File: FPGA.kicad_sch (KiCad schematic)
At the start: 2 parts

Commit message: added most of the sourcing info
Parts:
- D3: Source (none) -> https://onecall.farnell.com/multicomp-pro/ss13l/schottky-re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
- FPGA1: Source (none) -> completed it mate
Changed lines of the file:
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@@
+      (effects (font (size 1.27 1.27)) hide)
+    )
+    (property "Source" "https://onecall.farnell.com/multicomp-pro/ss13l/schottky-rect-single-30v-sod-123fl/dp/3883704" (id 4) (at 107.95 121.92 0)
       (effects (font (size 1.27 1.27)) hide)
     )
@@
       (effects (font (size 1.27 1.27)) hide)
     )
+    (property "Source" "completed it mate" (id 4) (at 140.97 87.63 0)
+      (effects (font (size 1.27 1.27)) hide)
+    )

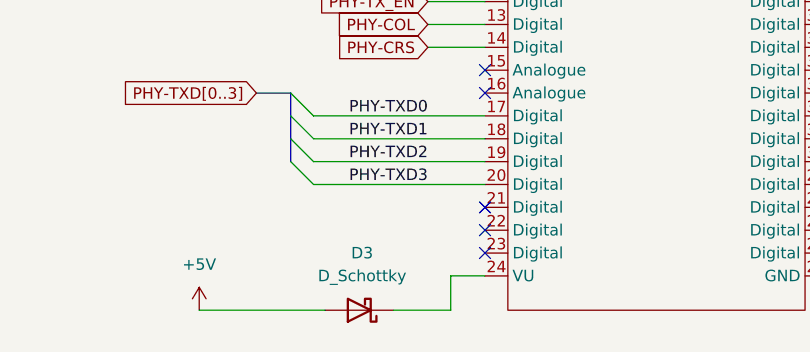
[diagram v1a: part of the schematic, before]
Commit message: solved power drc problems
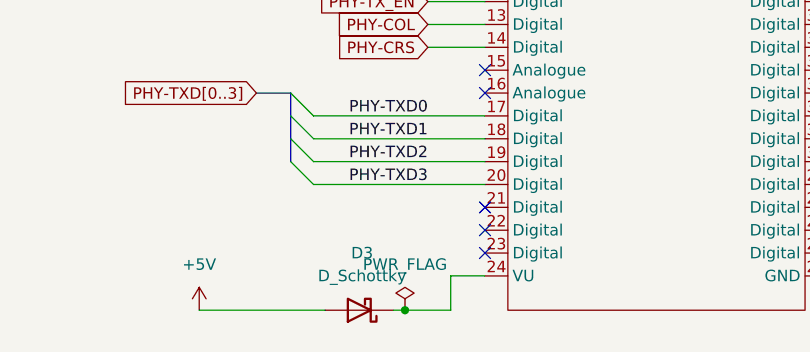
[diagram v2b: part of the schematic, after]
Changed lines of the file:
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@@
 (kicad_sch (version 20211123) (generator eeschema)
   (paper "A4")
+  (junction (at 113.03 121.92) (diameter 0) (color 0 0 0 0)
+  )
   (no_connect (at 160.02 95.25))
   (no_connect (at 121.92 97.79))
@@
     (stroke (width 0) (type default) (color 0 0 0 0))
   )
+  (wire (pts (xy 113.03 121.92) (xy 111.76 121.92))
+    (stroke (width 0) (type default) (color 0 0 0 0))
+  )
   (bus (pts (xy 91.44 64.77) (xy 91.44 67.31))
     (stroke (width 0) (type default) (color 0 0 0 0))
@@
     (stroke (width 0) (type default) (color 0 0 0 0))
   )
-  (wire (pts (xy 118.11 121.92) (xy 111.76 121.92))
+  (wire (pts (xy 118.11 121.92) (xy 113.03 121.92))
     (stroke (width 0) (type default) (color 0 0 0 0))
   )
@@
     (pin "9")
   )
+  (symbol (lib_id "power:PWR_FLAG") (at 113.03 121.92 0) (unit 1)
+    (in_bom yes) (on_board yes) (fields_autoplaced)
+    (property "Reference" "#FLG0111" (id 0) (at 113.03 120.015 0)
+      (effects (font (size 1.27 1.27)) hide)
+    )
+    (property "Value" "PWR_FLAG" (id 1) (at 113.03 116.84 0))
+    (property "Footprint" "" (id 2) (at 113.03 121.92 0)
+      (effects (font (size 1.27 1.27)) hide)
+    )
+    (property "Datasheet" "~" (id 3) (at 113.03 121.92 0)
+      (effects (font (size 1.27 1.27)) hide)
+    )
+    (pin "1")
+  )
   (symbol (lib_id "power:+5V") (at 90.17 121.92 0) (unit 1)

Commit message: Create PCB
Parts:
- FPGA1: footprint OUR_FOOTPRINTS:FPGA -> FPGA:FPGA
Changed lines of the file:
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@@
     (property "Reference" "FPGA1" (id 0) (at 140.97 34.29 0))
     (property "Value" "Artix-7 Dev Board" (id 1) (at 140.97 36.83 0))
-    (property "Footprint" "OUR_FOOTPRINTS:FPGA" (id 2) (at 140.97 87.63 0)
+    (property "Footprint" "FPGA:FPGA" (id 2) (at 140.97 87.63 0)
       (effects (font (size 1.27 1.27)) hide)
     )

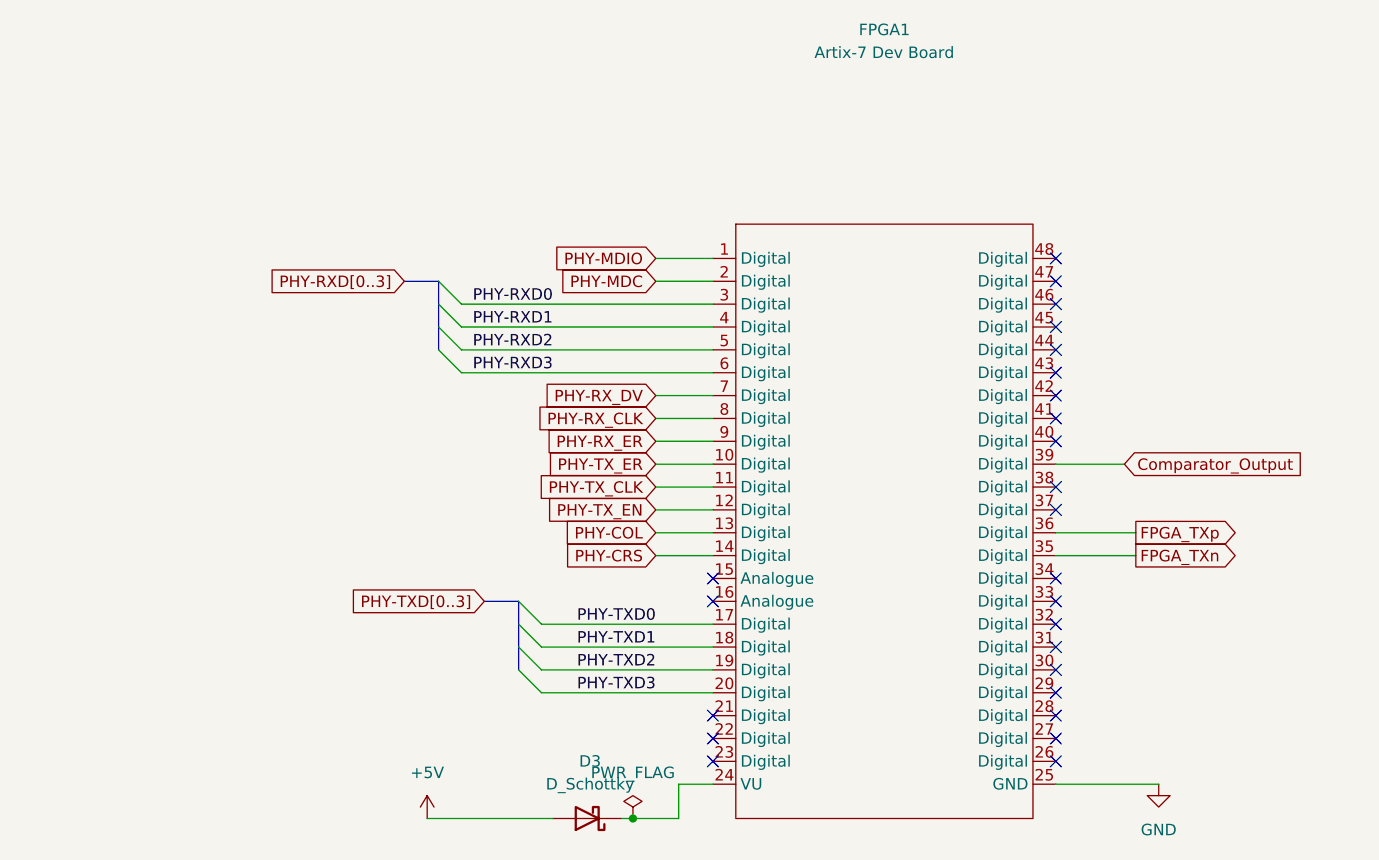
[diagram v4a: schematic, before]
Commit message: moved some resitors around to make myself feel better
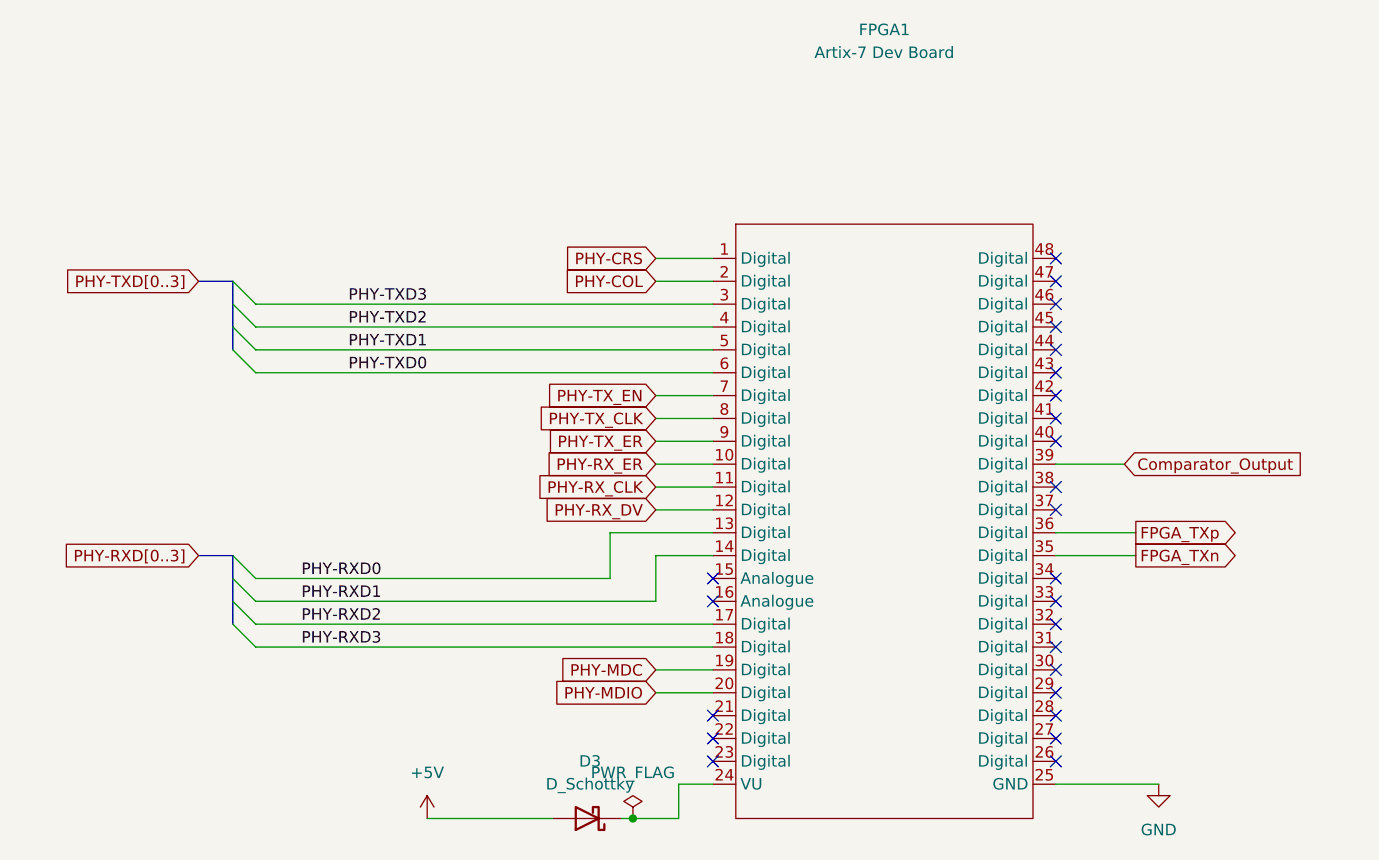
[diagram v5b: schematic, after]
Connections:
- net PHY-COL: now also FPGA1.2 (Digital); no longer FPGA1.13 (Digital)
- net PHY-CRS: now also FPGA1.1 (Digital); no longer FPGA1.14 (Digital)
- net PHY-MDC: now also FPGA1.19 (Digital); no longer FPGA1.2 (Digital)
- net PHY-MDIO: now also FPGA1.20 (Digital); no longer FPGA1.1 (Digital)
- net PHY-RXD0: now also FPGA1.13 (Digital); no longer FPGA1.3 (Digital)
- net PHY-RXD1: now also FPGA1.14 (Digital); no longer FPGA1.4 (Digital)
- net PHY-RXD2: now also FPGA1.17 (Digital); no longer FPGA1.5 (Digital)
- net PHY-RXD3: now also FPGA1.18 (Digital); no longer FPGA1.6 (Digital)
- net PHY-RX_CLK: now also FPGA1.11 (Digital); no longer FPGA1.8 (Digital)
- net PHY-RX_DV: now also FPGA1.12 (Digital); no longer FPGA1.7 (Digital)
- net PHY-RX_ER: now also FPGA1.10 (Digital); no longer FPGA1.9 (Digital)
- net PHY-TXD0: now also FPGA1.6 (Digital); no longer FPGA1.17 (Digital)
- net PHY-TXD1: now also FPGA1.5 (Digital); no longer FPGA1.18 (Digital)
- net PHY-TXD2: now also FPGA1.4 (Digital); no longer FPGA1.19 (Digital)
- net PHY-TXD3: now also FPGA1.3 (Digital); no longer FPGA1.20 (Digital)
- net PHY-TX_CLK: now also FPGA1.8 (Digital); no longer FPGA1.11 (Digital)
- net PHY-TX_EN: now also FPGA1.7 (Digital); no longer FPGA1.12 (Digital)
- net PHY-TX_ER: now also FPGA1.9 (Digital); no longer FPGA1.10 (Digital)

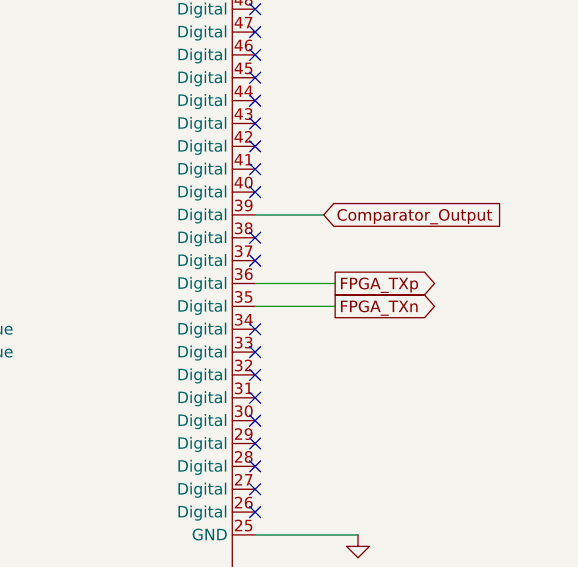
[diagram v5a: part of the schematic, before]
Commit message: Place and route optic side parts
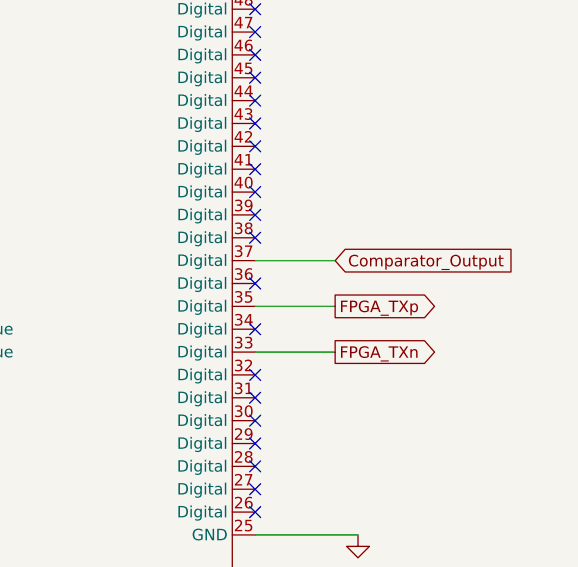
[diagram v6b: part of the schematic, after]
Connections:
- net Comparator_Output: now also FPGA1.37 (Digital); no longer FPGA1.39 (Digital)
- net FPGA_TXn: now also FPGA1.33 (Digital); no longer FPGA1.35 (Digital)
- net FPGA_TXp: now also FPGA1.35 (Digital); no longer FPGA1.36 (Digital)
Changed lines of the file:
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@@
   (no_connect (at 160.02 85.09))
   (no_connect (at 160.02 77.47))
-  (no_connect (at 160.02 97.79))
+  (no_connect (at 160.02 90.17))
   (no_connect (at 121.92 95.25))
   (no_connect (at 160.02 115.57))
   (no_connect (at 160.02 67.31))
   (no_connect (at 160.02 62.23))
-  (no_connect (at 160.02 87.63))
   (no_connect (at 121.92 115.57))
   (no_connect (at 160.02 113.03))
@@
   (no_connect (at 160.02 72.39))
   (no_connect (at 160.02 74.93))
+  (no_connect (at 160.02 82.55))
   (no_connect (at 160.02 69.85))
   (no_connect (at 160.02 80.01))
@@
     (stroke (width 0) (type default) (color 0 0 0 0))
   )
+  (wire (pts (xy 90.17 121.92) (xy 104.14 121.92))
+    (stroke (width 0) (type default) (color 0 0 0 0))
+  )
+  (wire (pts (xy 115.57 82.55) (xy 121.92 82.55))
+    (stroke (width 0) (type default) (color 0 0 0 0))
+  )
+  (wire (pts (xy 115.57 87.63) (xy 121.92 87.63))
+    (stroke (width 0) (type default) (color 0 0 0 0))
+  )
+  (wire (pts (xy 110.49 90.17) (xy 110.49 95.25))
+    (stroke (width 0) (type default) (color 0 0 0 0))
+  )
+  (wire (pts (xy 121.92 90.17) (xy 110.49 90.17))
+    (stroke (width 0) (type default) (color 0 0 0 0))
+  )
+  (bus (pts (xy 64.77 62.23) (xy 68.58 62.23))
+    (stroke (width 0) (type default) (color 0 0 0 0))
+  )
+  (wire (pts (xy 71.12 69.85) (xy 121.92 69.85))
+    (stroke (width 0) (type default) (color 0 0 0 0))
+  )
+  (wire (pts (xy 71.12 100.33) (xy 121.92 100.33))
+    (stroke (width 0) (type default) (color 0 0 0 0))
+  )
+  (bus (pts (xy 68.58 62.23) (xy 68.58 64.77))
+    (stroke (width 0) (type default) (color 0 0 0 0))
+  )
+  (bus (pts (xy 68.58 95.25) (xy 68.58 92.71))
+    (stroke (width 0) (type default) (color 0 0 0 0))
+  )
+  (wire (pts (xy 71.12 64.77) (xy 121.92 64.77))
+    (stroke (width 0) (type default) (color 0 0 0 0))
+  )
   (wire (pts (xy 160.02 92.71) (xy 168.91 92.71))
     (stroke (width 0) (type default) (color 0 0 0 0))
   )
-  (wire (pts (xy 90.17 121.92) (xy 104.14 121.92))
-    (stroke (width 0) (type default) (color 0 0 0 0))
-  )
-  (wire (pts (xy 115.57 82.55) (xy 121.92 82.55))
-    (stroke (width 0) (type default) (color 0 0 0 0))
-  )
-  (wire (pts (xy 115.57 87.63) (xy 121.92 87.63))
-    (stroke (width 0) (type default) (color 0 0 0 0))
-  )
-  (wire (pts (xy 110.49 90.17) (xy 110.49 95.25))
-    (stroke (width 0) (type default) (color 0 0 0 0))
-  )
-  (wire (pts (xy 121.92 90.17) (xy 110.49 90.17))
-    (stroke (width 0) (type default) (color 0 0 0 0))
-  )
-  (bus (pts (xy 64.77 62.23) (xy 68.58 62.23))
-    (stroke (width 0) (type default) (color 0 0 0 0))
-  )
-  (wire (pts (xy 71.12 69.85) (xy 121.92 69.85))
-    (stroke (width 0) (type default) (color 0 0 0 0))
-  )
-  (wire (pts (xy 71.12 100.33) (xy 121.92 100.33))
-    (stroke (width 0) (type default) (color 0 0 0 0))
-  )
-  (bus (pts (xy 68.58 62.23) (xy 68.58 64.77))
-    (stroke (width 0) (type default) (color 0 0 0 0))
-  )
-  (bus (pts (xy 68.58 95.25) (xy 68.58 92.71))
-    (stroke (width 0) (type default) (color 0 0 0 0))
-  )
-  (wire (pts (xy 160.02 90.17) (xy 168.91 90.17))
-    (stroke (width 0) (type default) (color 0 0 0 0))
-  )
-  (wire (pts (xy 71.12 64.77) (xy 121.92 64.77))
-    (stroke (width 0) (type default) (color 0 0 0 0))
-  )
   (wire (pts (xy 113.03 121.92) (xy 111.76 121.92))
     (stroke (width 0) (type default) (color 0 0 0 0))
@@
     (stroke (width 0) (type default) (color 0 0 0 0))
   )
-  (wire (pts (xy 160.02 82.55) (xy 167.64 82.55))
-    (stroke (width 0) (type default) (color 0 0 0 0))
-  )
   (wire (pts (xy 115.57 97.79) (xy 71.12 97.79))
     (stroke (width 0) (type default) (color 0 0 0 0))
@@
     (stroke (width 0) (type default) (color 0 0 0 0))
   )
+  (wire (pts (xy 160.02 97.79) (xy 168.91 97.79))
+    (stroke (width 0) (type default) (color 0 0 0 0))
+  )
   (wire (pts (xy 121.92 118.11) (xy 118.11 118.11))
     (stroke (width 0) (type default) (color 0 0 0 0))
@@
     (stroke (width 0) (type default) (color 0 0 0 0))
   )
+  (wire (pts (xy 160.02 87.63) (xy 168.91 87.63))
+    (stroke (width 0) (type default) (color 0 0 0 0))
+  )
   (label "PHY-TXD3" (at 90.17 64.77 180)
     (effects (font (size 1.27 1.27)) (justify right bottom))
@@
     )
   )
-  (global_label "Comparator_Output" (shape input) (at 167.64 82.55 0) (fields_autoplaced)
+  (global_label "Comparator_Output" (shape input) (at 168.91 87.63 0) (fields_autoplaced)
     (effects (font (size 1.27 1.27)) (justify left))
-    (property "Intersheet References" "${INTERSHEET_REFS}" (id 0) (at 188.2564 82.4706 0)
+    (property "Intersheet References" "${INTERSHEET_REFS}" (id 0) (at 189.5264 87.5506 0)
       (effects (font (size 1.27 1.27)) (justify left) hide)
     )
@@
     )
   )
-  (global_label "FPGA_TXp" (shape output) (at 168.91 90.17 0) (fields_autoplaced)
-    (effects (font (size 1.27 1.27)) (justify left))
-    (property "Intersheet References" "${INTERSHEET_REFS}" (id 0) (at 180.3341 90.0906 0)
-      (effects (font (size 1.27 1.27)) (justify left) hide)
-    )
-  )
-  (global_label "FPGA_TXn" (shape output) (at 168.91 92.71 0) (fields_autoplaced)
+  (global_label "FPGA_TXp" (shape output) (at 168.91 92.71 0) (fields_autoplaced)
     (effects (font (size 1.27 1.27)) (justify left))
     (property "Intersheet References" "${INTERSHEET_REFS}" (id 0) (at 180.3341 92.6306 0)
       (effects (font (size 1.27 1.27)) (justify left) hide)
     )
+  )
+  (global_label "FPGA_TXn" (shape output) (at 168.91 97.79 0) (fields_autoplaced)
+    (effects (font (size 1.27 1.27)) (justify left))
+    (property "Intersheet References" "${INTERSHEET_REFS}" (id 0) (at 180.3341 97.7106 0)
+      (effects (font (size 1.27 1.27)) (justify left) hide)
+    )

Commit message: did lots of routing for phy
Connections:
- net PHY-COL: now also FPGA1.17 (Digital); no longer FPGA1.2 (Digital)
- net PHY-CRS: now also FPGA1.18 (Digital); no longer FPGA1.1 (Digital)
- net PHY-MDC: now also FPGA1.2 (Digital); no longer FPGA1.19 (Digital)
- net PHY-MDIO: now also FPGA1.1 (Digital); no longer FPGA1.20 (Digital)
- net PHY-RXD0: now also FPGA1.6 (Digital); no longer FPGA1.13 (Digital)
- net PHY-RXD1: now also FPGA1.5 (Digital); no longer FPGA1.14 (Digital)
- net PHY-RXD2: now also FPGA1.4 (Digital); no longer FPGA1.17 (Digital)
- net PHY-RXD3: now also FPGA1.3 (Digital); no longer FPGA1.18 (Digital)
- net PHY-RX_CLK: now also FPGA1.8 (Digital); no longer FPGA1.11 (Digital)
- net PHY-RX_DV: now also FPGA1.7 (Digital); no longer FPGA1.12 (Digital)
- net PHY-RX_ER: now also FPGA1.9 (Digital); no longer FPGA1.10 (Digital)
- net PHY-TXD0: now also FPGA1.13 (Digital); no longer FPGA1.6 (Digital)
- net PHY-TXD1: now also FPGA1.14 (Digital); no longer FPGA1.5 (Digital)
- net PHY-TXD2: now also FPGA1.15 (Analogue); no longer FPGA1.4 (Digital)
- net PHY-TXD3: now also FPGA1.16 (Analogue); no longer FPGA1.3 (Digital)
- net PHY-TX_CLK: now also FPGA1.11 (Digital); no longer FPGA1.8 (Digital)
- net PHY-TX_EN: now also FPGA1.12 (Digital); no longer FPGA1.7 (Digital)
- net PHY-TX_ER: now also FPGA1.10 (Digital); no longer FPGA1.9 (Digital)
- no-connect marks 25 -> 23

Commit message: did a lot more routing, phy nearly done
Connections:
- no-connect marks 23 -> 25
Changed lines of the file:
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@@
   (no_connect (at 160.02 77.47))
   (no_connect (at 160.02 90.17))
+  (no_connect (at 121.92 107.95))
+  (no_connect (at 121.92 105.41))
   (no_connect (at 160.02 115.57))
   (no_connect (at 160.02 67.31))
